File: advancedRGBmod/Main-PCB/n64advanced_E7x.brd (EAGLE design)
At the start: 64.5 x 37.7 mm, 109 parts, among them J6 UPS, U1 10CL010YE144, U2 ADV7125/ADV7123, U4 74LVC3G34, U5 S25FLXXXSO8-DUAL, U6 TLV70012DDC, U7 TLV70025DDC

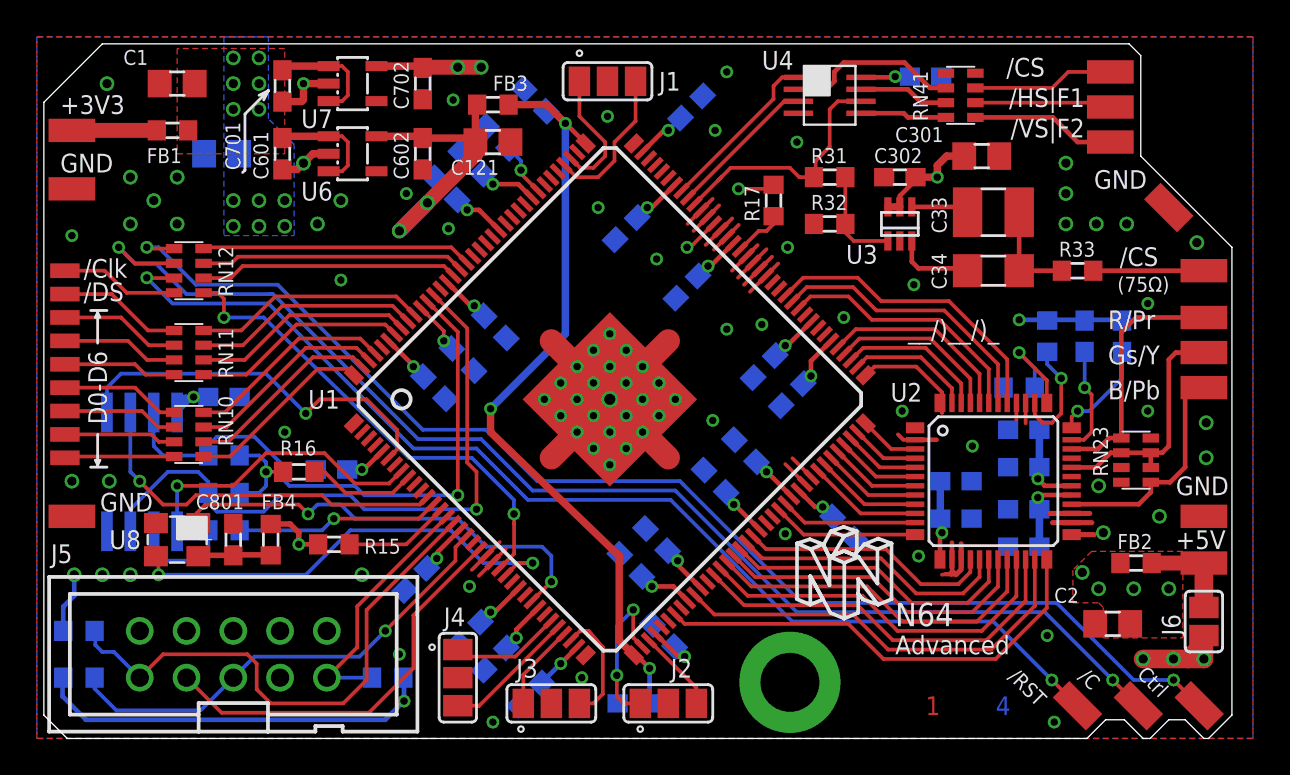
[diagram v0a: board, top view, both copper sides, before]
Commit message: PCB Update: - unused VREF to VCCIO (see connection guideline) - unused DEV_CLRn and DEV_OE to GND (see connection guideline) - rename of some resistors
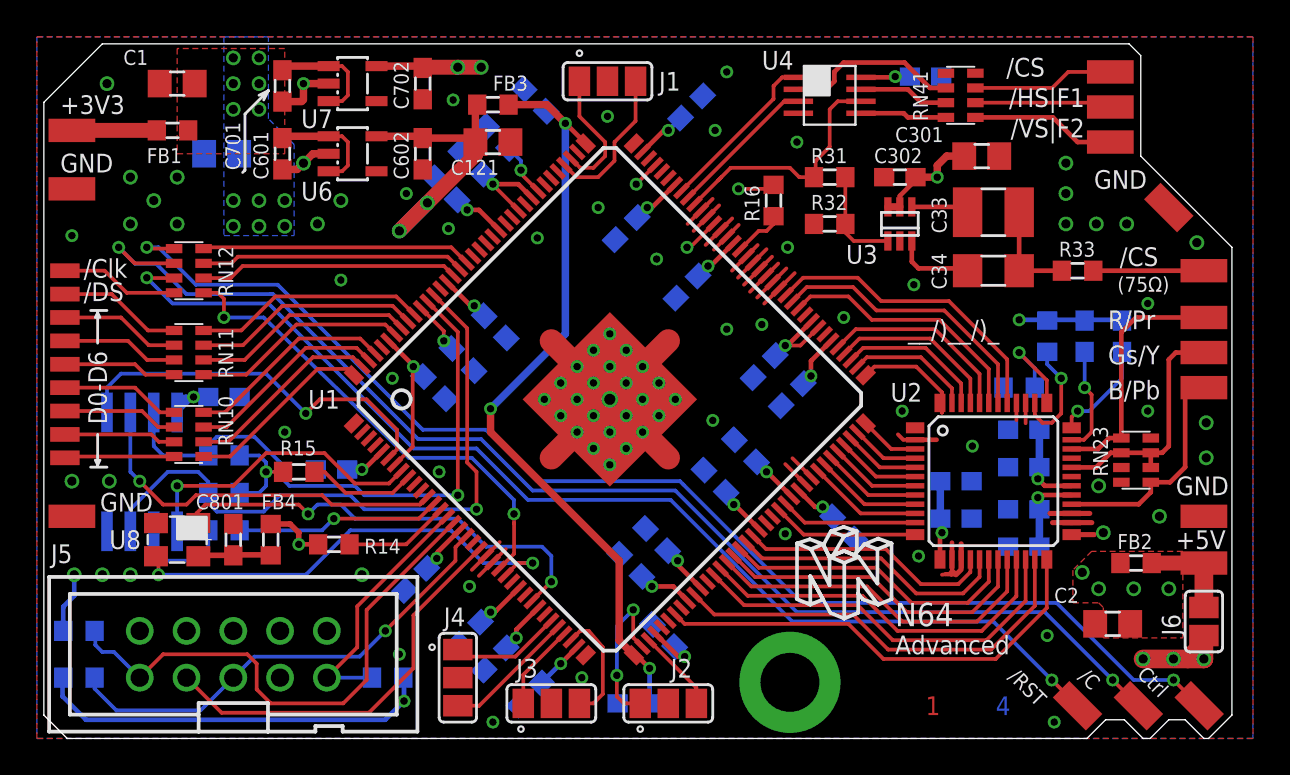
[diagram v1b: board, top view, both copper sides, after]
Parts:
- removed R17: 10k, rcl:R0603
- added R14: 10k, rcl:R0603
- moved R16 29.7 mm to (40.0, 29.2), turned to 270 degrees
- moved R15 4.37 mm to (14.2, 14.5)
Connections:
- net GND: now also U1.86, U1.87
- net N$45: now also R15.1; no longer R16.1
- net N$52: now also R16.2; no longer R17.2
- net N$8: now also R14.1; no longer R15.1
- net VCCIO: now also R14.2, R16.1, U1.105, U1.119, U1.7, U1.80; no longer R16.2, R17.1
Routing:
- net VCCIO: track 96.0 -> 107.5 mm, vias 31 -> 32
- net GND: track 66.9 -> 71.5 mm, vias 81 -> 84
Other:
- board text added: "N64A_20171012"
- board text added: "R14"
- board text removed: "N64A_20170923"
- board text removed: "R17"
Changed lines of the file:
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@@
 <text x="5.969" y="31.242" size="0.8128" layer="25" font="vector" ratio="15">FB1</text>
 <text x="4.699" y="36.576" size="0.8128" layer="25" font="vector" ratio="15">C1</text>
-<text x="13.208" y="15.367" size="0.8128" layer="25" font="vector" ratio="15">R16</text>
-<text x="17.78" y="10.033" size="0.8128" layer="25" font="vector" ratio="15">R15</text>
+<text x="13.208" y="15.367" size="0.8128" layer="25" font="vector" ratio="15">R15</text>
+<text x="17.78" y="10.033" size="0.8128" layer="25" font="vector" ratio="15">R14</text>
 <text x="13.843" y="10.795" size="0.8128" layer="26" font="vector" ratio="15" rot="MR0">R51</text>
 <text x="0.762" y="9.525" size="1.016" layer="25" font="vector" ratio="15">J5</text>
@@
 <text x="49.403" y="24.384" size="0.8128" layer="25" font="vector" ratio="15" rot="R90">C34</text>
 <text x="55.499" y="26.162" size="0.8128" layer="25" font="vector" ratio="15">R33</text>
-<text x="39.243" y="28.067" size="0.8128" layer="25" font="vector" ratio="15" rot="R90">R17</text>
+<text x="39.243" y="28.067" size="0.8128" layer="25" font="vector" ratio="15" rot="R90">R16</text>
 <text x="42.037" y="31.242" size="0.8128" layer="25" font="vector" ratio="15">R31</text>
 <text x="42.037" y="28.702" size="0.8128" layer="25" font="vector" ratio="15">R32</text>
@@
 <circle x="32.766" y="0.508" radius="0.05679375" width="0.3048" layer="25"/>
 <circle x="29.464" y="37.211" radius="0.05679375" width="0.3048" layer="25"/>
-<text x="10.668" y="1.27" size="1.016" layer="26" font="vector" ratio="12" rot="MR0" align="center">N64A_20170923</text>
+<text x="10.668" y="1.27" size="1.016" layer="26" font="vector" ratio="12" rot="MR0" align="center">N64A_20171012</text>
 <wire x1="11.303" y1="30.861" x2="11.303" y2="33.909" width="0.1524" layer="25"/>
 <wire x1="11.303" y1="33.909" x2="12.573" y2="35.179" width="0.1524" layer="25"/>
@@
 <element name="R12" library="rcl" package="R0603" value="10k" x="2.286" y="3.302" smashed="yes" rot="MR0"/>
 <element name="R13" library="rcl" package="R0603" value="10k" x="19.05" y="3.302" smashed="yes" rot="MR180"/>
-<element name="R15" library="rcl" package="R0603" value="10k" x="16.129" y="10.541" smashed="yes" rot="R180"/>
-<element name="R16" library="rcl" package="R0603" value="10k" x="14.224" y="14.478" smashed="yes" rot="R180"/>
-<element name="R17" library="rcl" package="R0603" value="10k" x="40.005" y="29.21" smashed="yes" rot="R270"/>
+<element name="R14" library="rcl" package="R0603" value="10k" x="16.129" y="10.541" smashed="yes" rot="R180"/>
+<element name="R15" library="rcl" package="R0603" value="10k" x="14.224" y="14.478" smashed="yes" rot="R180"/>
+<element name="R16" library="rcl" package="R0603" value="10k" x="40.005" y="29.21" smashed="yes" rot="R270"/>
 <element name="R51" library="rcl" package="R0603" value="25" x="10.16" y="11.303" smashed="yes" rot="MR180"/>
 <element name="R21" library="rcl" package="R0603" value="530/560" x="53.34" y="19.05" smashed="yes" rot="MR0"/>
@@
 <wire x1="28.702" y1="33.401" x2="28.702" y2="21.971" width="0.4064" layer="16"/>
 <via x="24.638" y="17.907" extent="1-16" drill="0.4"/>
-<wire x1="31.623" y1="9.906" x2="31.623" y2="5.320496875" width="0.4064" layer="1"/>
-<wire x1="32.423146875" y1="4.52035" x2="31.623" y2="5.320496875" width="0.4064" layer="1"/>
+<wire x1="31.623" y1="5.320496875" x2="32.423146875" y2="4.52035" width="0.4064" layer="1"/>
 <via x="33.274" y="3.81" extent="1-16" drill="0.4"/>
 <wire x1="33.274" y1="3.81" x2="32.56365" y2="4.52035" width="0.254" layer="1"/>
@@
 <wire x1="28.702" y1="21.971" x2="24.638" y2="17.907" width="0.4064" layer="16"/>
 <wire x1="24.638" y1="17.907" x2="24.638" y2="16.637" width="0.4064" layer="1"/>
-<wire x1="24.638" y1="16.637" x2="31.623" y2="9.906" width="0.4064" layer="1"/>
 <contactref element="U1" pad="37"/>
 <contactref element="U1" pad="109"/>
+<wire x1="24.638" y1="16.637" x2="31.623" y2="9.652" width="0.4064" layer="1"/>
+<wire x1="31.623" y1="9.652" x2="31.623" y2="5.320496875" width="0.4064" layer="1"/>
 </signal>
 <signal name="VCCIO">
@@
 <contactref element="C601" pad="1"/>
 <contactref element="J5" pad="4"/>
-<contactref element="R17" pad="1"/>
+<contactref element="R16" pad="1"/>
+<contactref element="R14" pad="2"/>
 <contactref element="R15" pad="2"/>
-<contactref element="R16" pad="2"/>
 <contactref element="C103" pad="1"/>
 <contactref element="C1" pad="1"/>
@@
 <wire x1="24.22304375" y1="30.64095625" x2="24.765" y2="30.099" width="0.254" layer="16"/>
 <wire x1="26.87235625" y1="29.375153125" x2="26.148509375" y2="30.099" width="0.254" layer="1"/>
-<wire x1="26.148509375" y1="30.099" x2="24.765" y2="30.099" width="0.254" layer="1"/>
+<wire x1="24.765" y1="30.099" x2="26.148509375" y2="30.099" width="0.254" layer="1"/>
 <wire x1="25.104590625" y1="27.6073875" x2="24.009978125" y2="28.702" width="0.254" layer="1"/>
 <wire x1="24.009978125" y1="28.702" x2="23.368" y2="28.702" width="0.254" layer="1"/>
 <via x="23.749" y="23.495" extent="1-16" drill="0.4"/>
 <via x="20.447" y="20.193" extent="1-16" drill="0.4"/>
-<wire x1="19.094184375" y1="21.596978125" x2="20.410821875" y2="20.280340625" width="0.254" layer="1"/>
+<wire x1="20.410821875" y1="20.280340625" x2="19.094184375" y2="21.596978125" width="0.254" layer="1"/>
 <wire x1="20.410821875" y1="20.280340625" x2="20.447" y2="20.193" width="0.254" layer="1" curve="-45"/>
 <wire x1="20.988959375" y1="19.651040625" x2="20.447" y2="20.193" width="0.254" layer="16"/>
@@
 <wire x1="40.64" y1="21.208996875" x2="40.64" y2="21.336" width="0.254" layer="16"/>
 <wire x1="42.075153125" y1="22.657640625" x2="40.767" y2="21.3494875" width="0.254" layer="1"/>
-<wire x1="40.767" y1="21.3494875" x2="40.64" y2="21.336" width="0.254" layer="1"/>
+<wire x1="40.64" y1="21.336" x2="40.767" y2="21.3494875" width="0.254" layer="1"/>
 <via x="8.509" y="18.542" extent="1-16" drill="0.4"/>
 <wire x1="9.31" y1="18.542" x2="8.509" y2="18.542" width="0.254" layer="16"/>
@@
 <wire x1="12.065" y1="13.335" x2="11.01" y2="13.335" width="0.2032" layer="16"/>
 <wire x1="12.065" y1="15.367" x2="11.01" y2="15.367" width="0.2032" layer="16"/>
+<contactref element="U1" pad="7"/>
+<contactref element="U1" pad="80"/>
+<contactref element="U1" pad="105"/>
+<contactref element="U1" pad="119"/>
+<wire x1="19.4477375" y1="14.879465625" x2="20.410821875" y2="15.84255" width="0.2032" layer="1"/>
+<wire x1="20.410821875" y1="15.84255" x2="20.410821875" y2="20.280340625" width="0.2032" layer="1"/>
+<wire x1="33.589871875" y1="31.142921875" x2="32.54595" y2="30.099" width="0.2032" layer="1"/>
+<via x="32.54595" y="30.099" extent="1-16" drill="0.4"/>
+<wire x1="26.16525" y1="28.668046875" x2="24.765" y2="30.068296875" width="0.2032" layer="1"/>
+<wire x1="24.765" y1="30.068296875" x2="24.765" y2="30.099" width="0.2032" layer="1"/>
+<wire x1="42.42870625" y1="22.304084375" x2="41.460621875" y2="21.336" width="0.2032" layer="1"/>
+<wire x1="41.460621875" y1="21.336" x2="40.64" y2="21.336" width="0.2032" layer="1"/>
 </signal>
 <signal name="VCCA">
@@
 <contactref element="U5" pad="4"/>
 <via x="22.352" y="27.686" extent="1-16" drill="0.4"/>
+<contactref element="U1" pad="87"/>
+<contactref element="U1" pad="86"/>
+<wire x1="39.116" y1="23.941125" x2="39.953834375" y2="24.778959375" width="0.2032" layer="1"/>
+<wire x1="39.497" y1="23.61501875" x2="40.3073875" y2="24.42540625" width="0.2032" layer="1"/>
+<wire x1="40.3073875" y1="24.42540625" x2="41.15498125" y2="25.273" width="0.2032" layer="1"/>
+<wire x1="39.953834375" y1="24.778959375" x2="40.701875" y2="25.527" width="0.2032" layer="1"/>
+<via x="21.844" y="14.478" extent="1-16" drill="0.4"/>
+<via x="27.178" y="27.178" extent="1-16" drill="0.4"/>
+<via x="19.304" y="19.558" extent="1-16" drill="0.4"/>
 </signal>
 <signal name="N$54">
@@
 <signal name="N$52">
 <contactref element="U1" pad="92"/>
-<contactref element="R17" pad="2"/>
+<contactref element="R16" pad="2"/>
 <wire x1="38.186065625" y1="26.546725" x2="39.198340625" y2="27.559" width="0.2032" layer="1"/>
 <wire x1="39.198340625" y1="27.559" x2="39.624" y2="27.559" width="0.2032" layer="1"/>
@@
 <signal name="N$45">
 <contactref element="U1" pad="9"/>
-<contactref element="R16" pad="1"/>
+<contactref element="R15" pad="1"/>
 <wire x1="20.15484375" y1="14.17235625" x2="19.3174875" y2="13.335" width="0.2032" layer="1"/>
 <wire x1="16.764" y1="13.335" x2="15.621" y2="14.478" width="0.2032" layer="1"/>
@@
 <signal name="N$8">
 <contactref element="U1" pad="14"/>
-<contactref element="R15" pad="1"/>
+<contactref element="R14" pad="1"/>
 <wire x1="16.979" y1="10.541" x2="20.05901875" y2="10.541" width="0.2032" layer="1"/>
 <wire x1="20.05901875" y1="10.541" x2="21.922609375" y2="12.404590625" width="0.2032" layer="1"/>

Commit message: important BOM update: Use Schmitt triggered buffer instead of simple one!!!
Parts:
- U4: value 74LVC3G34 -> 74LVC3G17
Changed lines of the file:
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@@
 <attribute name="VALUE" x="49.403" y="27.94" size="1.016" layer="27" font="vector" ratio="12"/>
 </element>
-<element name="U4" library="OSSC_HDMI_Audio" package="74LVC3G34" value="74LVC3G34" x="43.053" y="34.925" smashed="yes"/>
+<element name="U4" library="OSSC_HDMI_Audio" package="74LVC3G34" value="74LVC3G17" x="43.053" y="34.925" smashed="yes"/>
 <element name="U6" library="v-reg-micrel" package="SOT23-5" value="TLV70012DDC" x="17.145" y="31.75" smashed="yes" rot="R270">
 <attribute name="MF" value="" x="17.145" y="31.75" size="1.778" layer="27" rot="R270" display="off"/>

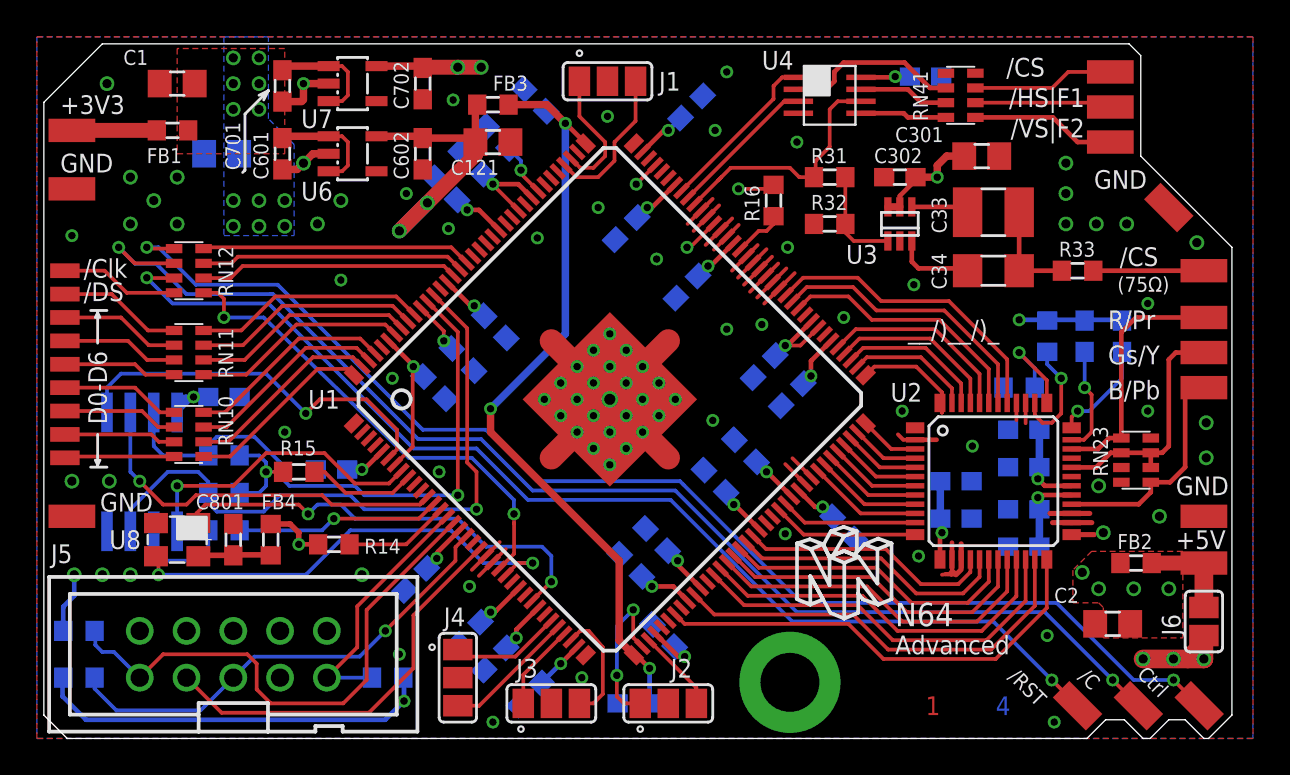
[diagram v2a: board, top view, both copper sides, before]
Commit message: Update PCB - reroute power supply layer reducing noise injection to +5V plane from digital signals - adapt some component positions
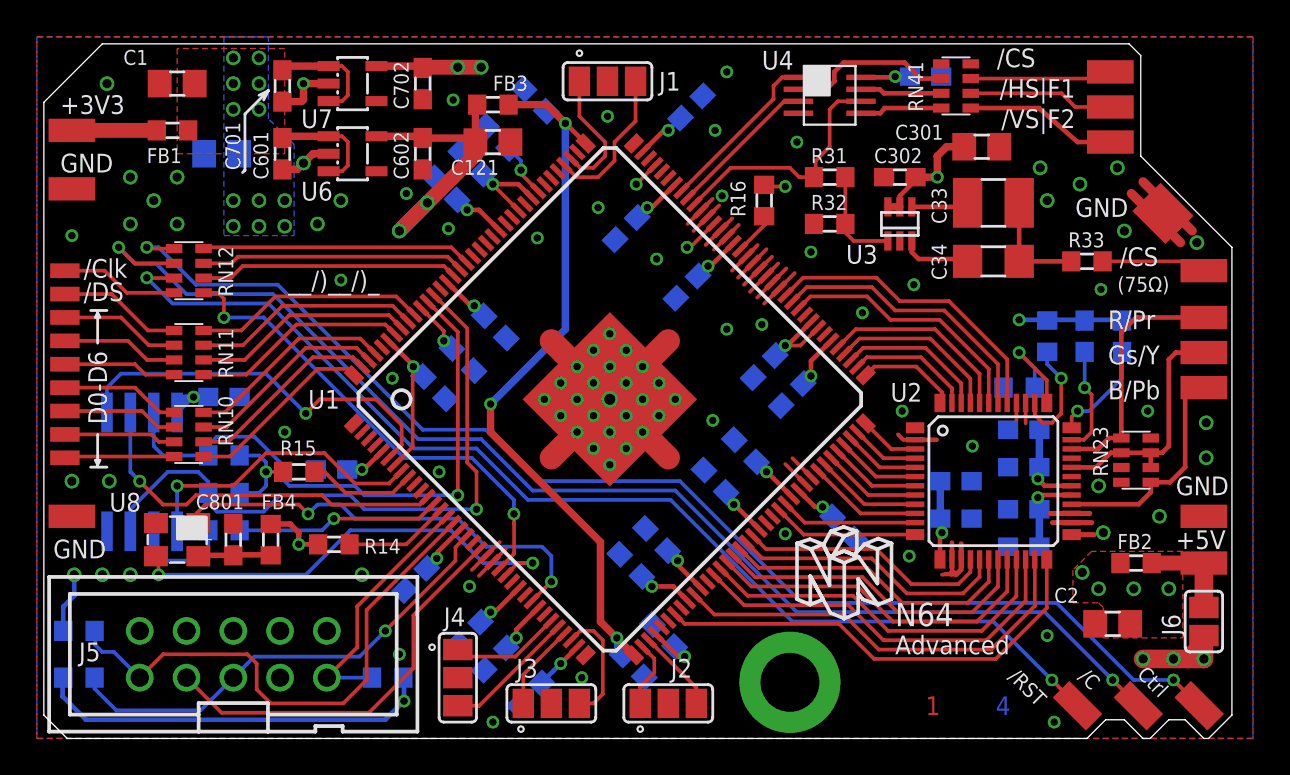
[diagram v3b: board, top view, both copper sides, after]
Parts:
- added P_GND4: (no value), wirepad:SMD1,27-2,54
- added U$1: (no value), logo:ESD_10.00
- added U$2: (no value), logo:MUELLTONNE_10.00
- moved C131 2.03 mm to (32.4, 3.94), turned to 225 degrees
- moved R33 0.72 mm to (57.0, 25.9)
- moved RN41 0.57 mm to (49.9, 35.4)
- moved C34 0.51 mm to (51.9, 25.9)
- moved R16 0.51 mm to (39.5, 29.2)
- moved C301 0.51 mm to (51.3, 32.1)
- moved C33 0.51 mm to (51.9, 29.1)
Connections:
- net GND: now also P_GND4.1
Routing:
- net VCCIO: track 107.5 -> 84.7 mm
- net GND: track 71.5 -> 78.9 mm, vias 84 -> 85
- net VCCA: track 111.9 -> 106.7 mm
- net RGSB#: track 8.71 -> 3.66 mm, vias 2 -> 0
- net VCCD_PLL: track 43.2 -> 41.3 mm
- net N$40: track 6.56 -> 5.62 mm
- net N$76: track 21.0 -> 21.5 mm
- net +5V: track 28.5 -> 29.0 mm
- net N$16: track 4.36 -> 3.85 mm
- net N$17: track 5.50 -> 6.00 mm
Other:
- board text added: "N64A_20171017"
- board text removed: "N64A_20171012"
